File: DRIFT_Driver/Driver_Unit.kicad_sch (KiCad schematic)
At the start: 28 parts, among them IC1 DRV8313RHHR, U1 INA199xxDCK, U2 74HC32

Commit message: Finished majority of component implementations
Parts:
- removed C1, C2, C5: 0.1uF, symbol Device:C
- removed C4: 0.01uF, symbol Device:C
- removed C6: 0.47uF, symbol Device:C
- added C1: 0.47u, Capacitor_SMD:C_0402_1005Metric, symbol Device:C_Small
- added C12: 0.01u, Capacitor_SMD:C_0402_1005Metric, symbol Device:C_Small
- added C2, C30, C8: 0.1u, Capacitor_SMD:C_0402_1005Metric, symbol Device:C_Small
- C3: footprint (none) -> Capacitor_SMD:C_0402_1005Metric
- IC1: footprint QFN50P600X600X100-37N-D -> Touchstone:QFN50P600X600X100-37N-D
- R1: renamed from R8; footprint (none) -> Resistor_SMD:R_0402_1005Metric
- R10: renamed from R4; footprint (none) -> Resistor_SMD:R_0402_1005Metric
- R11: renamed from R5; footprint (none) -> Resistor_SMD:R_0402_1005Metric
- R12: renamed from R6; footprint (none) -> Resistor_SMD:R_0402_1005Metric
- R2: renamed from R10; footprint (none) -> Resistor_SMD:R_0402_1005Metric
- R3: renamed from R12; footprint (none) -> Resistor_SMD:R_0402_1005Metric
- R4: renamed from R7; footprint (none) -> Resistor_SMD:R_0402_1005Metric
- R5: renamed from R9; footprint (none) -> Resistor_SMD:R_0402_1005Metric
- R6: renamed from R11; footprint (none) -> Resistor_SMD:R_0402_1005Metric
- R8: renamed from R3; footprint (none) -> Resistor_SMD:R_0402_1005Metric
- U1: renamed from U2; footprint (none) -> Package_SO:SOIC-14_3.9x8.7mm_P1.27mm
- renumbered C5 to C6, C5 to C7, C5 to C9, R98 to R13, R1 to R7, R1 to R9, U1 to U2, U1 to U3
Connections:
- net GNDS is gone; now on net GND: C6.1, C9.1, U2.1 (REF), U2.2 (GND), U3.1 (REF), U3.2 (GND)
- net +3.3V: now also C1.2
- net GND: now also C1.1, C30.1, C8.1
- net VMOT: now also C2.1, C30.2, C8.2
- net at IC1.5 (CPL): now also C12.2
- net at IC1.6 (CPH): now also C12.1
- net at IC1.7 (VCP): now also C2.2
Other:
- moved on the sheet: C3, C5, C6, C7, C9, IC1, R1, R10, R11, R12, R13, R2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

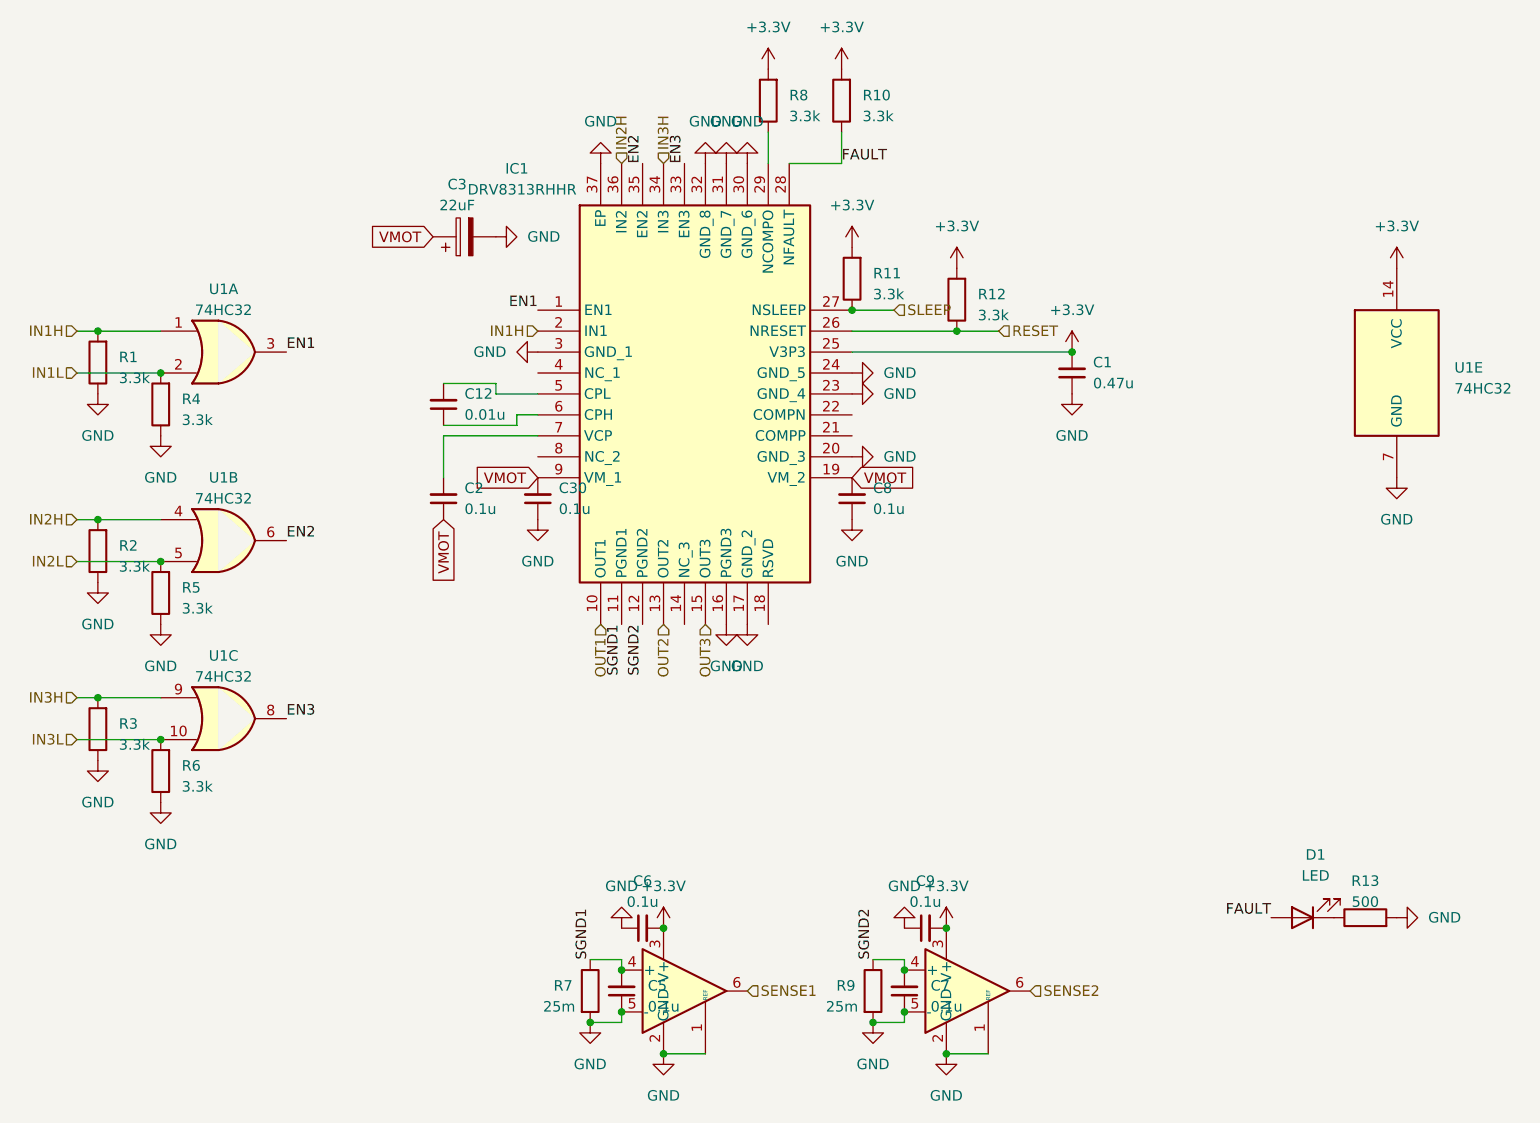
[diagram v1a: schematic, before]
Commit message: Changed annotations and fixed capacitor ratings
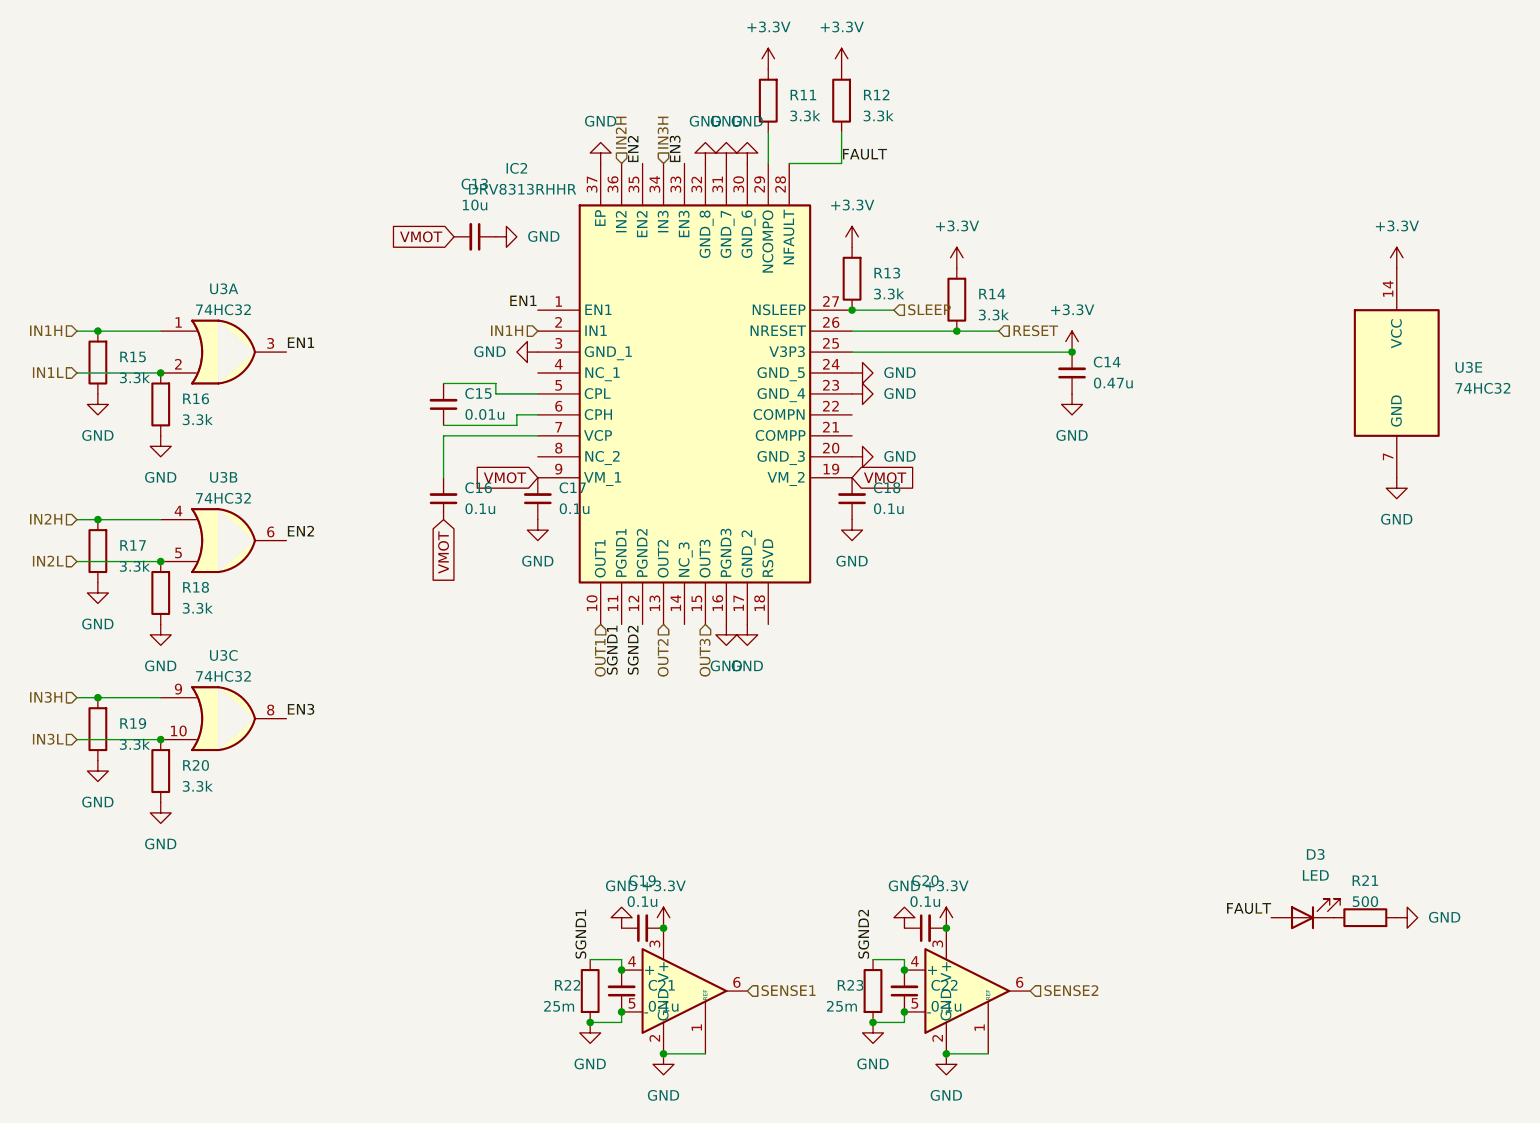
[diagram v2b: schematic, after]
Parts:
- removed C3: 22uF, Capacitor_SMD:C_0402_1005Metric, symbol Device:C_Polarized
- added C13: 10u, Capacitor_SMD:C_0805_2012Metric, symbol Device:C_Small
- renumbered C1 to C14, C12 to C15, C2 to C16, C30 to C17, C8 to C18, C6 to C19, C9 to C20, C5 to C21, C7 to C22, D1 to D3, IC1 to IC2, R8 to R11, R10 to R12, R11 to R13, R12 to R14, R1 to R15, R4 to R16, R2 to R17, R5 to R18, R3 to R19, R6 to R20, R13 to R21, R7 to R22, R9 to R23, U1 to U3, U2 to U4, U3 to U5
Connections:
- net GND: now also C13.1
- net VMOT: now also C13.2

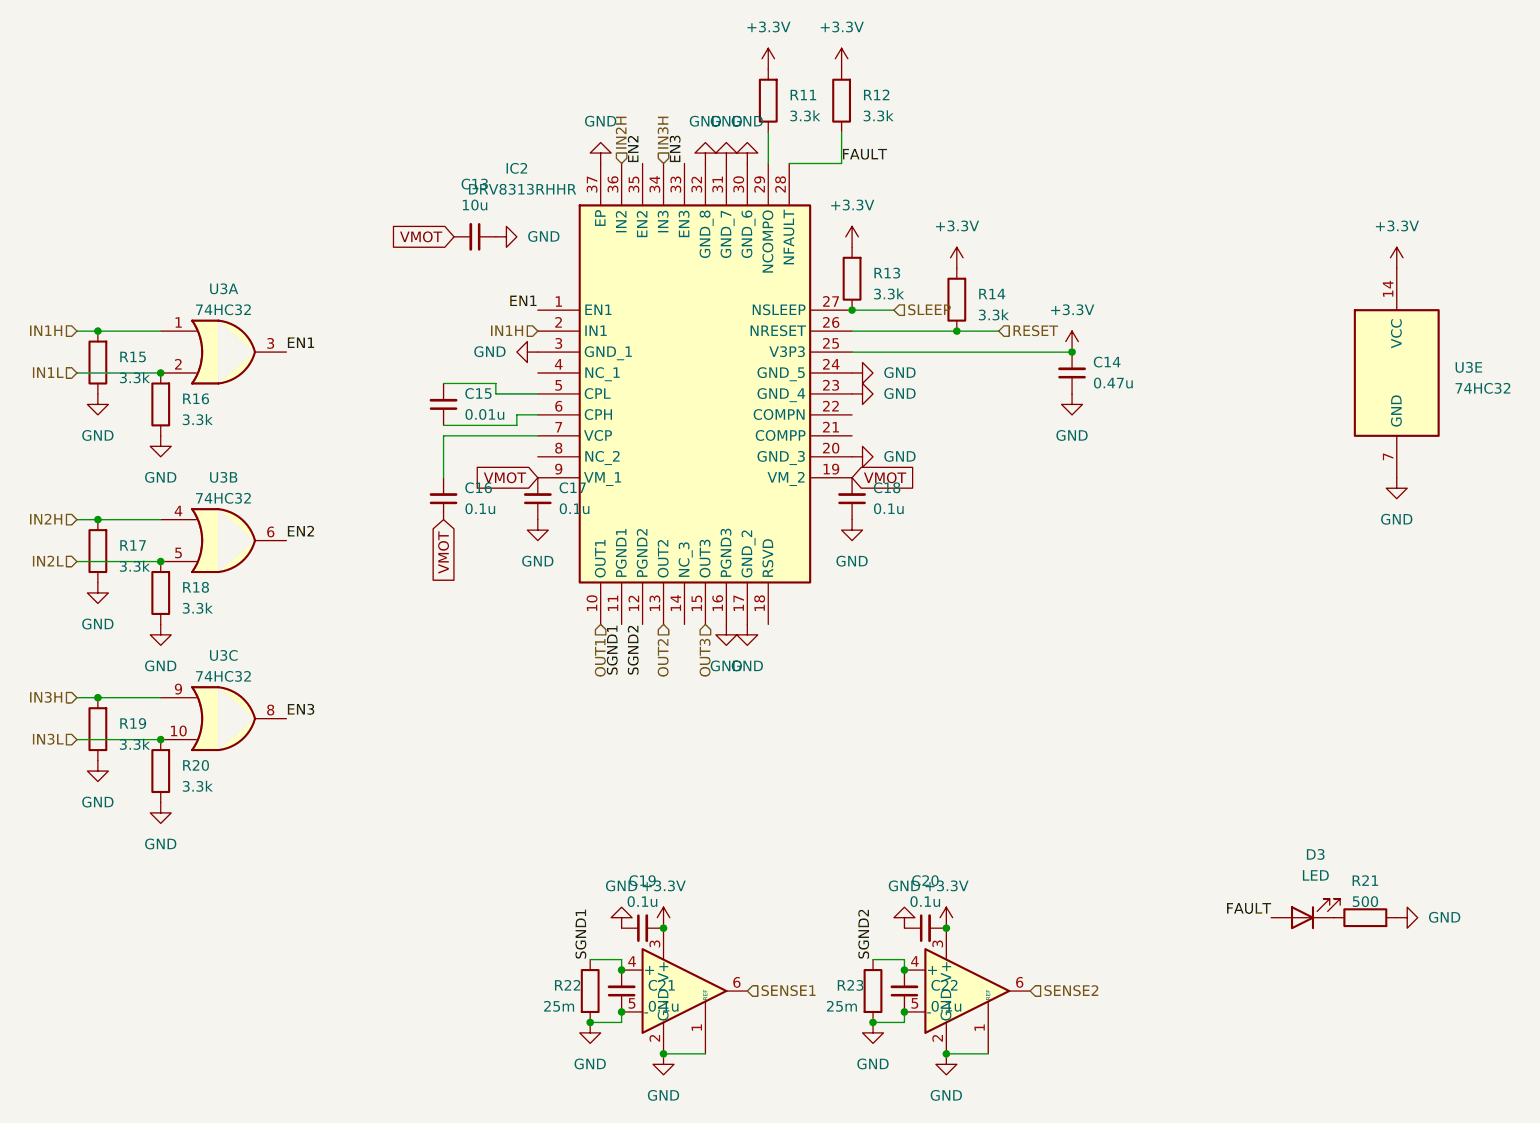
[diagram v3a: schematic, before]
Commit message: Some progress on motor driver unit layout
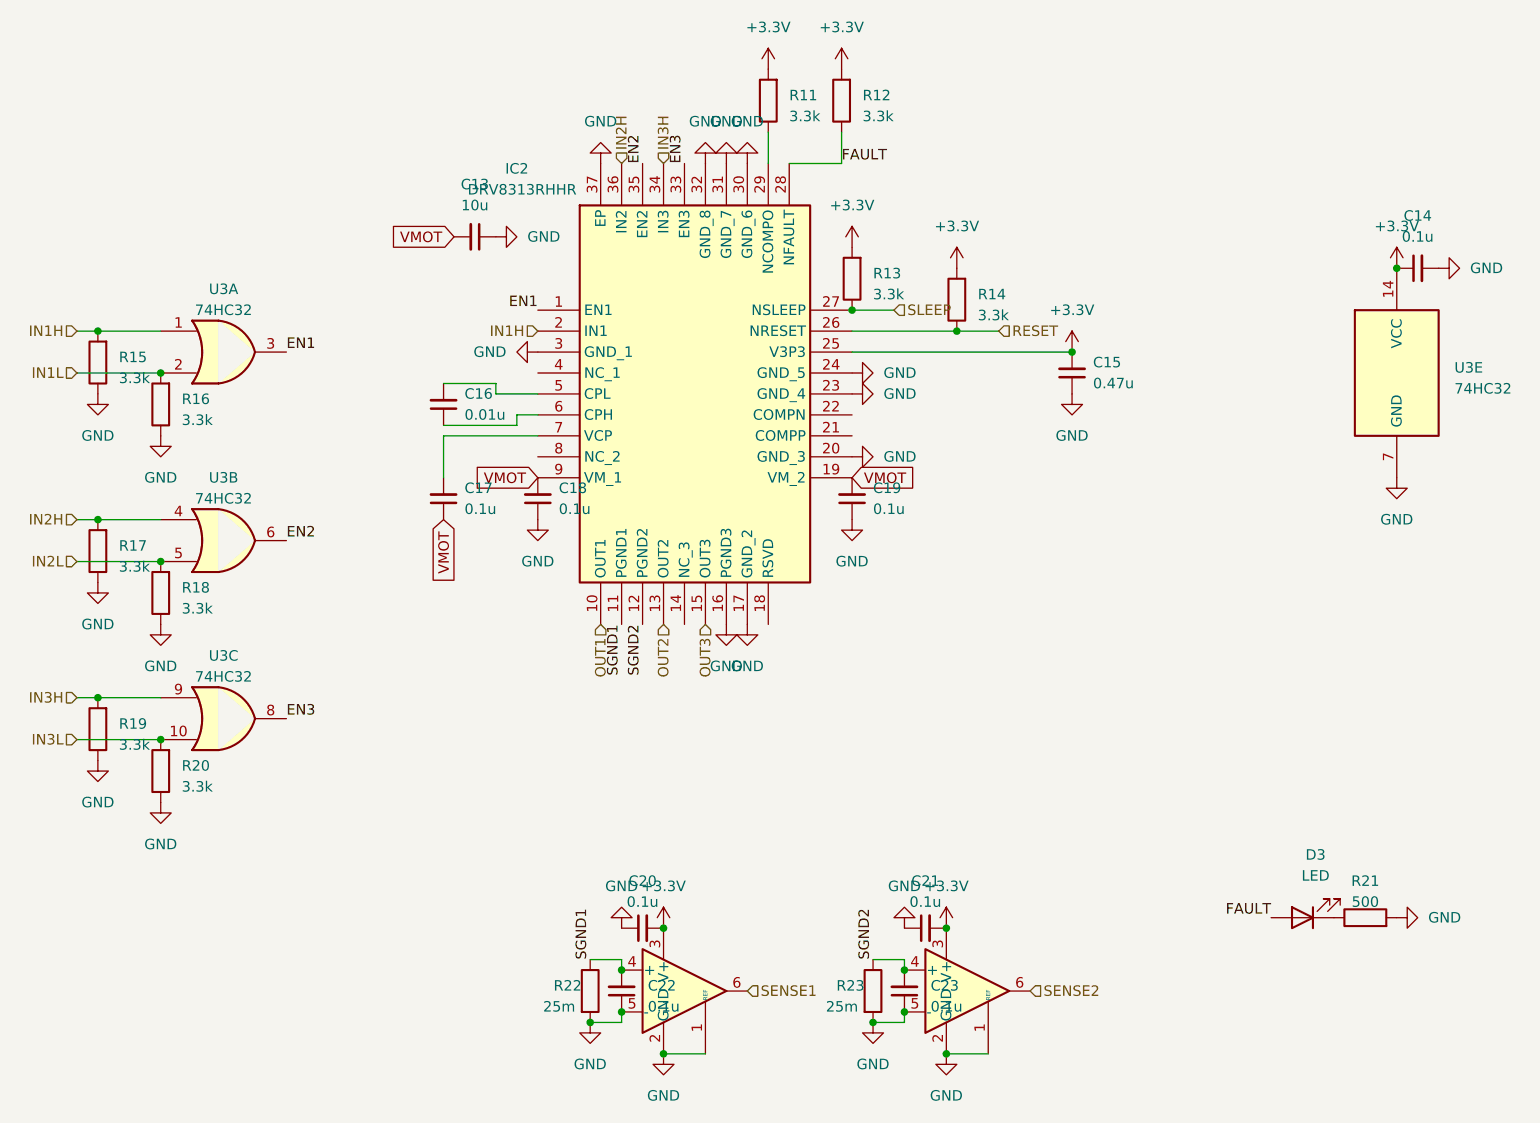
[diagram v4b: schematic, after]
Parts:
- added C14: 0.1u, Capacitor_SMD:C_0402_1005Metric, symbol Device:C_Small
- R22, R23: footprint Resistor_SMD:R_1206_3216Metric -> Resistor_SMD:R_0603_1608Metric
- renumbered C14 to C15, C15 to C16, C16 to C17, C17 to C18, C18 to C19, C19 to C20, C20 to C21, C21 to C22, C22 to C23
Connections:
- net +3.3V: now also C14.1
- net GND: now also C14.2
